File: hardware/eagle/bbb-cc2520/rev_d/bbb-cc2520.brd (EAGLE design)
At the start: 54.6 x 73.4 mm, 98 parts, among them J1 TC2030-IDC, J2 JUMPER-PTH-2-NO, P9/P8 BBB_HEADERS, U1 CC2520, U2 CC2520, U3 CAT24C256WI-GT3, U4 CC2591, U5 CD4051B-53B, U6 NRF51822QF, X1 NX2520SA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

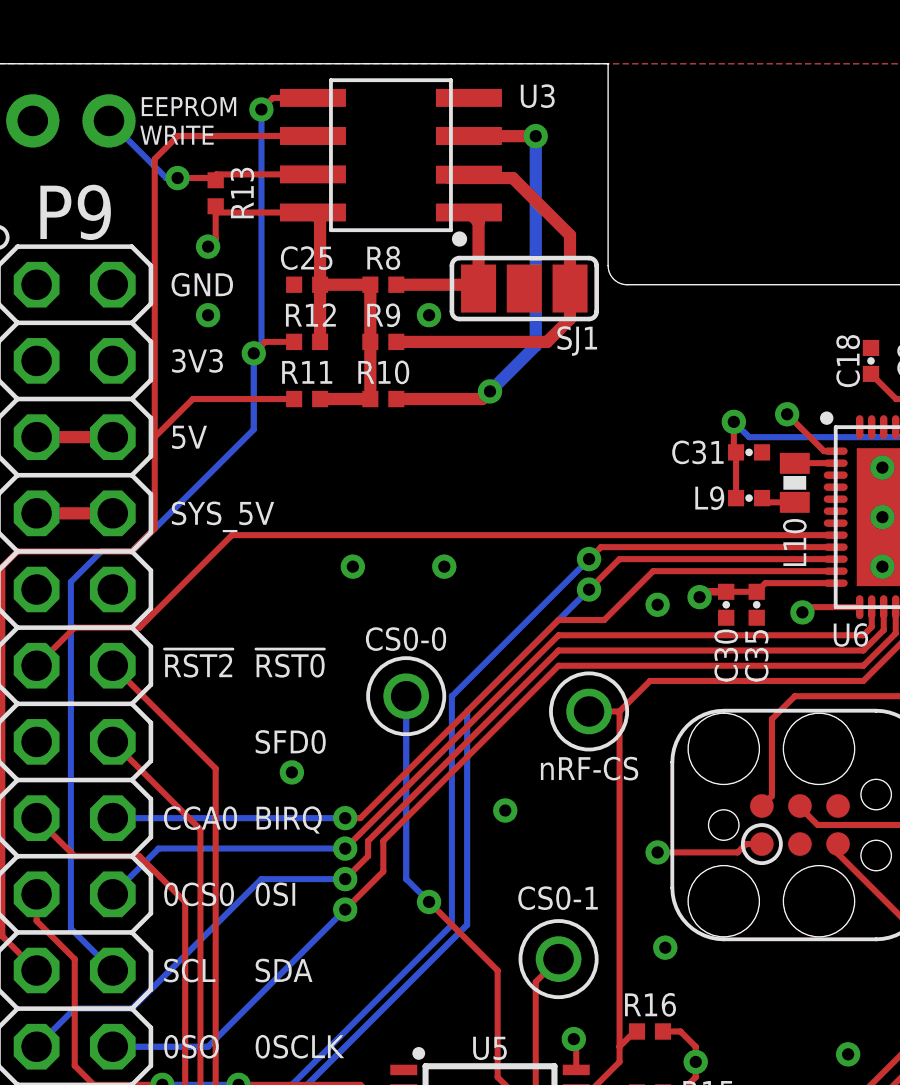
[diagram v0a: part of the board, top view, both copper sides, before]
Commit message: moved cs0 pin
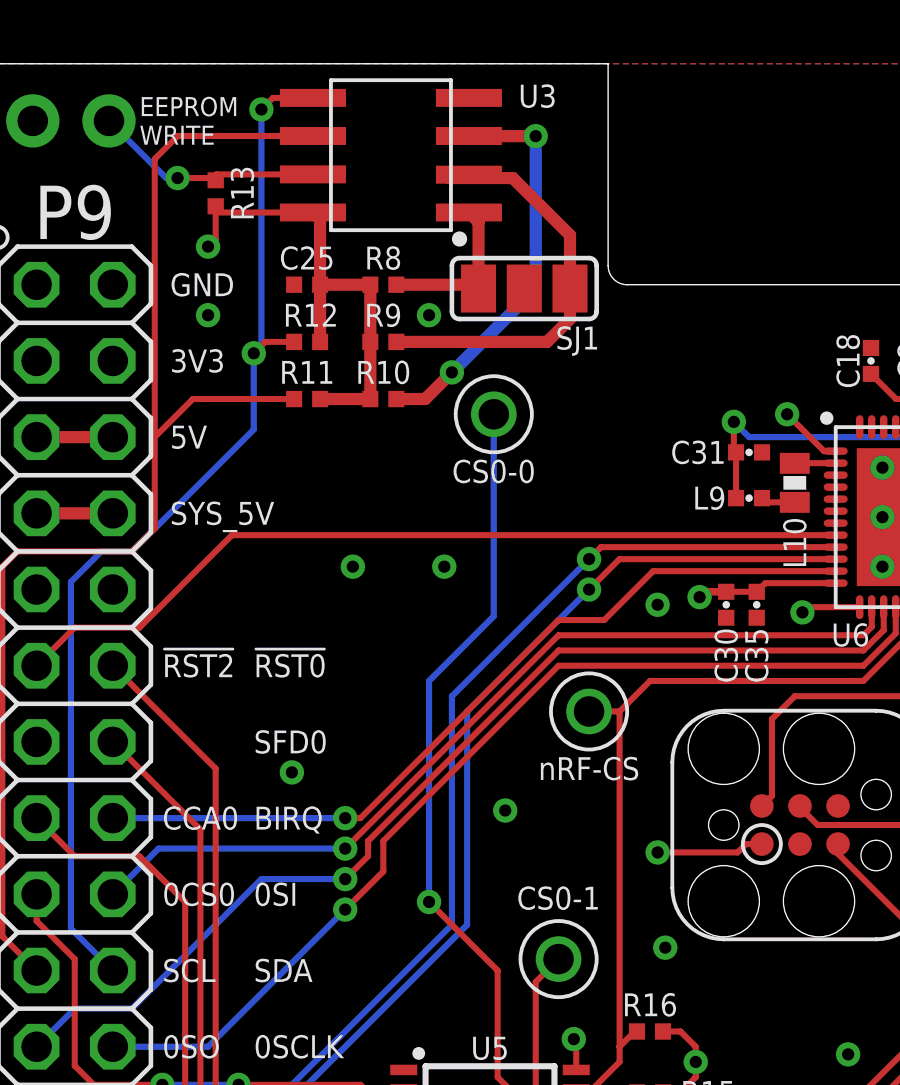
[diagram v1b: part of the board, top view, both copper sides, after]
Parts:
- moved TP0 9.84 mm to (17.1, 61.7)
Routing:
- net SPI0_CS0_0: track 20.6 -> 30.6 mm
- net N$32: track 14.6 -> 13.5 mm
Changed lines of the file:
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@@
 WRITE</text>
 <text x="19.304" y="45.212" size="0.762" layer="21" font="vector" ratio="12" align="bottom-center">CS0-1</text>
-<text x="14.224" y="53.848" size="0.762" layer="21" font="vector" ratio="12" align="bottom-center">CS0-0</text>
+<text x="17.145" y="60.198" size="0.762" layer="21" font="vector" ratio="12" rot="R180" align="bottom-center">CS0-0</text>
 <text x="20.32" y="50.292" size="0.762" layer="21" font="vector" ratio="12" rot="R180" align="bottom-center">nRF-CS</text>
 <text x="14.478" y="32.258" size="0.762" layer="21" font="vector" ratio="12" rot="R180" align="bottom-center">CS0-3</text>
@@
 <attribute name="VALUE" x="47.498" y="67.818" size="0.762" layer="27" font="vector" ratio="10" rot="R90" align="top-center"/>
 </element>
-<element name="TP0" library="headers" package="TESTPOINT_0.040IN" value="TEST_POINT_0.040IN" x="14.224" y="52.324" smashed="yes">
-<attribute name="DIGIKEY" value="5001K-ND" x="14.224" y="52.324" size="1.778" layer="27" display="off"/>
-<attribute name="VALUE" x="14.224" y="49.784" size="1.016" layer="27" font="vector" ratio="12" align="bottom-center"/>
+<element name="TP0" library="headers" package="TESTPOINT_0.040IN" value="TEST_POINT_0.040IN" x="17.145" y="61.722" smashed="yes">
+<attribute name="DIGIKEY" value="5001K-ND" x="17.145" y="61.722" size="1.778" layer="27" display="off"/>
+<attribute name="VALUE" x="17.145" y="59.182" size="1.016" layer="27" font="vector" ratio="12" align="bottom-center"/>
 </element>
 <element name="TP1" library="headers" package="TESTPOINT_0.040IN" value="TEST_POINT_0.040IN" x="19.304" y="43.561" smashed="yes">
@@
 <contactref element="U3" pad="A2"/>
 <contactref element="R10" pad="1"/>
-<via x="17.018" y="62.484" extent="1-16" drill="0.4064"/>
+<via x="15.748" y="63.119" extent="1-16" drill="0.4064"/>
 <via x="18.542" y="70.993" extent="1-16" drill="0.4064"/>
 <wire x1="16.316" y1="70.998" x2="16.321" y2="70.993" width="0.4064" layer="1"/>
 <wire x1="16.321" y1="70.993" x2="18.542" y2="70.993" width="0.4064" layer="1"/>
-<wire x1="17.018" y1="62.484" x2="18.542" y2="64.008" width="0.4064" layer="16"/>
-<wire x1="18.542" y1="64.008" x2="18.542" y2="70.993" width="0.4064" layer="16"/>
-<wire x1="13.89506875" y1="62.23" x2="16.764" y2="62.23" width="0.4064" layer="1"/>
-<wire x1="16.764" y1="62.23" x2="17.018" y2="62.484" width="0.4064" layer="1"/>
+<wire x1="15.748" y1="63.119" x2="18.542" y2="65.913" width="0.4064" layer="16"/>
+<wire x1="18.542" y1="65.913" x2="18.542" y2="70.993" width="0.4064" layer="16"/>
+<wire x1="13.89506875" y1="62.23" x2="14.859" y2="62.23" width="0.4064" layer="1"/>
+<wire x1="14.859" y1="62.23" x2="15.748" y2="63.119" width="0.4064" layer="1"/>
 </signal>
 <signal name="SDA">
@@
 <contactref element="R14" pad="1"/>
 <contactref element="TP0" pad="TESTPOINT"/>
-<wire x1="14.224" y1="52.324" x2="14.224" y2="46.228" width="0.2032" layer="16"/>
-<wire x1="14.224" y1="46.228" x2="14.986" y2="45.466" width="0.2032" layer="16"/>
 <via x="14.986" y="45.466" extent="1-16" drill="0.4064"/>
 <wire x1="23.18893125" y1="37.846" x2="23.11793125" y2="37.917" width="0.2032" layer="1"/>
@@
 <wire x1="17.272" y1="39.624" x2="18.979" y2="37.917" width="0.2032" layer="1"/>
 <wire x1="18.979" y1="37.917" x2="19.893" y2="37.917" width="0.2032" layer="1"/>
+<wire x1="14.986" y1="45.466" x2="14.986" y2="52.832" width="0.2032" layer="16"/>
+<wire x1="14.986" y1="52.832" x2="17.145" y2="54.991" width="0.2032" layer="16"/>
+<wire x1="17.145" y1="54.991" x2="17.145" y2="61.722" width="0.2032" layer="16"/>
 </signal>
 <signal name="!RESET1">

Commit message: committing changes to gap
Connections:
- removed net A0: U6.45
- removed net A1: U6.46
- removed net CC0_GPIO0: U1.10
- removed net CC0_GPIO5: U1.4
- removed net P03: U6.7
- removed net P12: U6.18
- removed net P24: U6.43
- removed net P25: U6.44
- removed net PROG_RX: U6.47
- removed net PROG_TX: U6.48
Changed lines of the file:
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@@
 <wire x1="13.462" y1="46.482" x2="12.192" y2="45.212" width="0.2032" layer="1"/>
-</signal>
-<signal name="CC0_GPIO5">
-<contactref element="U1" pad="4"/>
-</signal>
-<signal name="CC0_GPIO0">
-<contactref element="U1" pad="10"/>
 </signal>
 <signal name="VCC">
@@
 <wire x1="26.19593125" y1="56.093" x2="25.908" y2="55.80506875" width="0.2032" layer="1"/>
 <wire x1="25.908" y1="55.80506875" x2="24.892" y2="55.80506875" width="0.2032" layer="1"/>
-<contactref element="R15" pad="2"/>
-<contactref element="R16" pad="2"/>
-<via x="23.876" y="40.132" extent="1-16" drill="0.4064"/>
-<contactref element="R14" pad="2"/>
 <wire x1="13.02893125" y1="66.04" x2="11.35506875" y2="66.04" width="0.4064" layer="1"/>
 <wire x1="11.35506875" y1="64.135" x2="11.35506875" y2="66.04" width="0.4064" layer="1"/>
@@
 <via x="24.003" y="55.626" extent="1-16" drill="0.4064"/>
 <wire x1="7.884" y1="68.448" x2="7.874" y2="68.65493125" width="0.254" layer="1"/>
+<wire x1="32.58693125" y1="19.05" x2="32.3215" y2="18.78456875" width="0.2032" layer="1"/>
+<wire x1="32.3215" y1="18.78456875" x2="32.3215" y2="17.78" width="0.2032" layer="1"/>
+<wire x1="11.35506875" y1="66.04" x2="11.35506875" y2="68.20893125" width="0.4064" layer="1"/>
+<wire x1="11.35506875" y1="68.20893125" x2="11.116" y2="68.448" width="0.4064" layer="1"/>
+<wire x1="19.812" y1="40.894" x2="19.893" y2="40.813" width="0.2032" layer="1"/>
+<wire x1="19.893" y1="40.813" x2="19.893" y2="39.867" width="0.2032" layer="1"/>
+<contactref element="R15" pad="2"/>
+<contactref element="R16" pad="2"/>
+<contactref element="R14" pad="2"/>
+<via x="23.876" y="40.132" extent="1-16" drill="0.4064"/>
 <wire x1="24.05506875" y1="37.846" x2="24.05506875" y2="38.42893125" width="0.2032" layer="1"/>
 <wire x1="24.05506875" y1="38.42893125" x2="23.368" y2="39.116" width="0.2032" layer="1"/>
 <wire x1="23.368" y1="39.116" x2="22.78506875" y2="39.116" width="0.2032" layer="1"/>
 <wire x1="22.78506875" y1="41.148" x2="23.368" y2="41.148" width="0.2032" layer="1"/>
-<wire x1="32.58693125" y1="19.05" x2="32.3215" y2="18.78456875" width="0.2032" layer="1"/>
-<wire x1="32.3215" y1="18.78456875" x2="32.3215" y2="17.78" width="0.2032" layer="1"/>
-<wire x1="11.35506875" y1="66.04" x2="11.35506875" y2="68.20893125" width="0.4064" layer="1"/>
-<wire x1="11.35506875" y1="68.20893125" x2="11.116" y2="68.448" width="0.4064" layer="1"/>
 <wire x1="23.368" y1="41.148" x2="23.876" y2="40.64" width="0.2032" layer="1"/>
 <wire x1="23.876" y1="40.64" x2="23.876" y2="40.132" width="0.2032" layer="1"/>
 <wire x1="23.368" y1="39.116" x2="23.876" y2="39.624" width="0.2032" layer="1"/>
 <wire x1="23.876" y1="39.624" x2="23.876" y2="40.132" width="0.2032" layer="1"/>
-<wire x1="19.812" y1="40.894" x2="19.893" y2="40.813" width="0.2032" layer="1"/>
-<wire x1="19.893" y1="40.813" x2="19.893" y2="39.867" width="0.2032" layer="1"/>
 </signal>
 <signal name="LED2">
@@
 <wire x1="46.91506875" y1="67.38493125" x2="46.736" y2="67.38493125" width="0.4064" layer="1"/>
 </signal>
-<signal name="P12">
-<contactref element="U6" pad="18"/>
-</signal>
-<signal name="PROG_RX">
-<contactref element="U6" pad="47"/>
-</signal>
-<signal name="PROG_TX">
-<contactref element="U6" pad="48"/>
-</signal>
-<signal name="P25">
-<contactref element="U6" pad="44"/>
-</signal>
-<signal name="P24">
-<contactref element="U6" pad="43"/>
-</signal>
-<signal name="A1">
-<contactref element="U6" pad="46"/>
-</signal>
-<signal name="A0">
-<contactref element="U6" pad="45"/>
-</signal>
 <signal name="BIRQ">
 <contactref element="P9/P8" pad="P9_16"/>
@@
 <wire x1="22.457" y1="56.493" x2="20.828" y2="54.864" width="0.2032" layer="1"/>
 </signal>
-<signal name="P03">
-<contactref element="U6" pad="7"/>
-</signal>
 <signal name="SPI0_CS0_SEL0">

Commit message: mouse bites
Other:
- board size 54.6 x 73.4 mm -> 57.2 x 75.9 mm
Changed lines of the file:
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@@
 <setting verticaltext="up"/>
 </settings>
-<grid distance="10" unitdist="mil" unit="mil" style="lines" multiple="1" display="yes" altdistance="5" altunitdist="mil" altunit="mil"/>
+<grid distance="50" unitdist="mil" unit="mil" style="lines" multiple="1" display="yes" altdistance="5" altunitdist="mil" altunit="mil"/>
 <layers>
 <layer number="1" name="Top" color="4" fill="1" visible="yes" active="yes"/>
@@
 <layer number="20" name="Dimension" color="15" fill="1" visible="yes" active="yes"/>
 <layer number="21" name="tPlace" color="7" fill="1" visible="yes" active="yes"/>
-<layer number="22" name="bPlace" color="7" fill="1" visible="yes" active="yes"/>
+<layer number="22" name="bPlace" color="7" fill="1" visible="no" active="yes"/>
 <layer number="23" name="tOrigins" color="15" fill="1" visible="yes" active="yes"/>
-<layer number="24" name="bOrigins" color="15" fill="1" visible="yes" active="yes"/>
+<layer number="24" name="bOrigins" color="15" fill="1" visible="no" active="yes"/>
 <layer number="25" name="tNames" color="7" fill="1" visible="yes" active="yes"/>
-<layer number="26" name="bNames" color="7" fill="1" visible="yes" active="yes"/>
+<layer number="26" name="bNames" color="7" fill="1" visible="no" active="yes"/>
 <layer number="27" name="tValues" color="7" fill="1" visible="no" active="yes"/>
 <layer number="28" name="bValues" color="7" fill="1" visible="no" active="yes"/>
@@
 <layer number="43" name="vRestrict" color="2" fill="10" visible="no" active="yes"/>
 <layer number="44" name="Drills" color="7" fill="1" visible="no" active="yes"/>
-<layer number="45" name="Holes" color="7" fill="1" visible="no" active="yes"/>
-<layer number="46" name="Milling" color="3" fill="1" visible="no" active="yes"/>
+<layer number="45" name="Holes" color="7" fill="1" visible="yes" active="yes"/>
+<layer number="46" name="Milling" color="3" fill="1" visible="yes" active="yes"/>
 <layer number="47" name="Measures" color="7" fill="1" visible="no" active="yes"/>
 <layer number="48" name="Document" color="7" fill="1" visible="no" active="yes"/>
@@
 <board>
 <plain>
-<wire x1="0" y1="73.406" x2="0" y2="12.7" width="0" layer="20"/>
-<wire x1="0" y1="12.7" x2="12.7" y2="0" width="0" layer="20" curve="90"/>
-<wire x1="12.7" y1="0" x2="41.91" y2="0" width="0" layer="20"/>
-<wire x1="41.91" y1="0" x2="54.61" y2="12.7" width="0" layer="20" curve="90"/>
-<wire x1="54.61" y1="12.7" x2="54.61" y2="73.406" width="0" layer="20"/>
-<wire x1="54.61" y1="73.406" x2="38.735" y2="73.406" width="0" layer="20"/>
-<wire x1="38.735" y1="73.406" x2="38.735" y2="66.675" width="0" layer="20"/>
-<wire x1="38.735" y1="66.675" x2="38.1" y2="66.04" width="0" layer="20" curve="-90"/>
-<wire x1="38.1" y1="66.04" x2="21.59" y2="66.04" width="0" layer="20"/>
-<wire x1="21.59" y1="66.04" x2="20.955" y2="66.675" width="0" layer="20" curve="-90"/>
-<wire x1="20.955" y1="66.675" x2="20.955" y2="73.406" width="0" layer="20"/>
+<wire x1="0" y1="73.406" x2="0" y2="12.7" width="0" layer="46"/>
+<wire x1="0" y1="12.7" x2="12.7" y2="0" width="0" layer="46" curve="90"/>
+<wire x1="12.7" y1="0" x2="41.91" y2="0" width="0" layer="46"/>
+<wire x1="41.91" y1="0" x2="54.61" y2="12.7" width="0" layer="46" curve="90"/>
+<wire x1="54.61" y1="12.7" x2="54.61" y2="73.406" width="0" layer="46"/>
+<wire x1="54.61" y1="73.406" x2="38.735" y2="73.406" width="0" layer="46"/>
+<wire x1="38.735" y1="73.406" x2="38.735" y2="66.675" width="0" layer="46"/>
+<wire x1="38.735" y1="66.675" x2="38.1" y2="66.04" width="0" layer="46" curve="-90"/>
+<wire x1="38.1" y1="66.04" x2="21.59" y2="66.04" width="0" layer="46"/>
+<wire x1="21.59" y1="66.04" x2="20.955" y2="66.675" width="0" layer="46" curve="-90"/>
+<wire x1="20.955" y1="66.675" x2="20.955" y2="73.406" width="0" layer="46"/>
 <text x="6.35" y="4.191" size="0.762" layer="51" font="vector" ratio="10" rot="R90" align="top-center">SDA</text>
 <text x="6.35" y="6.731" size="0.762" layer="51" font="vector" ratio="10" rot="R90" align="top-center">SCL</text>
@@
 <text x="48.514" y="4.064" size="1.27" layer="21" font="vector" ratio="14" align="bottom-center">D</text>
 <text x="9.144" y="48.26" size="0.762" layer="25" font="vector" ratio="12" align="center-left">BIRQ</text>
-<wire x1="20.955" y1="73.406" x2="0" y2="73.406" width="0" layer="20"/>
+<wire x1="20.955" y1="73.406" x2="0" y2="73.406" width="0" layer="46"/>
 <text x="5.334" y="71.501" size="0.635" layer="21" font="vector" ratio="12" align="center-left">EEPROM
 WRITE</text>
@@
 <text x="9.144" y="30.48" size="0.762" layer="25" font="vector" ratio="12" align="center-left">1SI</text>
 <text x="6.35" y="27.94" size="0.762" layer="25" font="vector" ratio="12" align="center-left">1SCLK</text>
+<wire x1="0" y1="73.406" x2="0" y2="59.69" width="0" layer="20"/>
+<wire x1="0" y1="55.88" x2="0" y2="23.495" width="0" layer="20"/>
+<wire x1="0" y1="19.685" x2="0" y2="12.7" width="0" layer="20"/>
+<wire x1="0" y1="12.7" x2="12.7" y2="0" width="0" layer="20" curve="90"/>
+<wire x1="12.7" y1="0" x2="15.113" y2="0" width="0" layer="20"/>
+<wire x1="18.923" y1="0" x2="39.116" y2="0" width="0" layer="20"/>
+<wire x1="42.926" y1="0.040640625" x2="54.61" y2="12.7" width="0" layer="20" curve="85.5"/>
+<wire x1="54.61" y1="12.7" x2="54.61" y2="19.685" width="0" layer="20"/>
+<wire x1="54.61" y1="23.495" x2="54.61" y2="55.88" width="0" layer="20"/>
+<wire x1="54.61" y1="59.69" x2="54.61" y2="73.406" width="0" layer="20"/>
+<wire x1="54.61" y1="73.406" x2="42.926" y2="73.406" width="0" layer="20"/>
+<wire x1="39.116" y1="73.406" x2="38.735" y2="73.406" width="0" layer="20"/>
+<wire x1="38.735" y1="73.406" x2="38.735" y2="66.675" width="0" layer="20"/>
+<wire x1="38.735" y1="66.675" x2="38.1" y2="66.04" width="0" layer="20" curve="-90"/>
+<wire x1="38.1" y1="66.04" x2="21.59" y2="66.04" width="0" layer="20"/>
+<wire x1="21.59" y1="66.04" x2="20.955" y2="66.675" width="0" layer="20" curve="-90"/>
+<wire x1="20.955" y1="66.675" x2="20.955" y2="73.406" width="0" layer="20"/>
+<wire x1="20.955" y1="73.406" x2="18.923" y2="73.406" width="0" layer="20"/>
+<wire x1="15.113" y1="73.406" x2="0" y2="73.406" width="0" layer="20"/>
+<wire x1="0" y1="23.495" x2="-1.27" y2="22.225" width="0" layer="20" curve="-90"/>
+<wire x1="-1.27" y1="20.955" x2="0" y2="19.685" width="0" layer="20" curve="-90"/>
+<hole x="0" y="21.59" drill="0.508"/>
+<hole x="0" y="22.225" drill="0.508"/>
+<hole x="0" y="22.86" drill="0.508"/>
+<hole x="0" y="20.955" drill="0.508"/>
+<hole x="0" y="20.32" drill="0.508"/>
+<wire x1="0" y1="59.69" x2="-1.27" y2="58.42" width="0" layer="20" curve="-90"/>
+<wire x1="-1.27" y1="57.15" x2="0" y2="55.88" width="0" layer="20" curve="-90"/>
+<hole x="0" y="57.785" drill="0.508"/>
+<hole x="0" y="58.42" drill="0.508"/>
+<hole x="0" y="59.055" drill="0.508"/>
+<hole x="0" y="57.15" drill="0.508"/>
+<hole x="0" y="56.515" drill="0.508"/>
+<hole x="54.61" y="57.785" drill="0.508"/>
+<hole x="54.61" y="57.15" drill="0.508"/>
+<hole x="54.61" y="56.515" drill="0.508"/>
+<hole x="54.61" y="58.42" drill="0.508"/>
+<hole x="54.61" y="59.055" drill="0.508"/>
+<wire x1="54.61" y1="59.69" x2="55.88" y2="58.42" width="0" layer="20" curve="90"/>
+<wire x1="55.88" y1="57.15" x2="54.61" y2="55.88" width="0" layer="20" curve="90"/>
+<wire x1="54.61" y1="23.495" x2="55.88" y2="22.225" width="0" layer="20" curve="90"/>
+<wire x1="55.88" y1="20.955" x2="54.61" y2="19.685" width="0" layer="20" curve="90"/>
+<hole x="54.61" y="21.59" drill="0.508"/>
+<hole x="54.61" y="22.225" drill="0.508"/>
+<hole x="54.61" y="22.86" drill="0.508"/>
+<hole x="54.61" y="20.955" drill="0.508"/>
+<hole x="54.61" y="20.32" drill="0.508"/>
+<wire x1="39.116" y1="73.406" x2="40.386" y2="74.676" width="0" layer="20" curve="90"/>
+<wire x1="41.656" y1="74.676" x2="42.926" y2="73.406" width="0" layer="20" curve="90"/>
+<hole x="41.021" y="73.406" drill="0.508"/>
+<hole x="41.656" y="73.406" drill="0.508"/>
+<hole x="42.291" y="73.406" drill="0.508"/>
+<hole x="40.386" y="73.406" drill="0.508"/>
+<hole x="39.751" y="73.406" drill="0.508"/>
+<wire x1="15.113" y1="73.406" x2="16.383" y2="74.676" width="0" layer="20" curve="90"/>
+<wire x1="17.653" y1="74.676" x2="18.923" y2="73.406" width="0" layer="20" curve="90"/>
+<hole x="17.018" y="73.406" drill="0.508"/>
+<hole x="17.653" y="73.406" drill="0.508"/>
+<hole x="18.288" y="73.406" drill="0.508"/>
+<hole x="16.383" y="73.406" drill="0.508"/>
+<hole x="15.748" y="73.406" drill="0.508"/>
+<wire x1="18.923" y1="0" x2="17.653" y2="-1.27" width="0" layer="20" curve="90"/>
+<wire x1="16.383" y1="-1.27" x2="15.113" y2="0" width="0" layer="20" curve="90"/>
+<hole x="17.018" y="0" drill="0.508"/>
+<hole x="16.383" y="0" drill="0.508"/>
+<hole x="15.748" y="0" drill="0.508"/>
+<hole x="17.653" y="0" drill="0.508"/>
+<hole x="18.288" y="0" drill="0.508"/>
+<wire x1="42.926" y1="0.040640625" x2="41.656" y2="-1.27" width="0" layer="20" curve="87"/>
+<wire x1="40.386" y1="-1.27" x2="39.116" y2="0" width="0" layer="20" curve="90"/>
+<hole x="41.021" y="0" drill="0.508"/>
+<hole x="40.386" y="0" drill="0.508"/>
+<hole x="39.751" y="0" drill="0.508"/>
+<hole x="41.656" y="0" drill="0.508"/>
+<hole x="42.291" y="0" drill="0.508"/>
 </plain>
 <attributes>
